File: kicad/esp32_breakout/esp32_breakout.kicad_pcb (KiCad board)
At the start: 2 copper layers, 78 x 39 mm, 30 parts, among them J1 JST PH F, J10 JST PH F, J11 JST PH F, J2 JST PH F, J3 JST PH F, J4 DC-005 5.5x2.1mm, J5 Deans T-Plug M, J6 Header F, J7 Header F, J8 Header F, J9 JST PH F, Q1 BSS123, SW1 SS12D10, U1 ESP32 DEV KIT 30-pin, U2 Mini560-Pro

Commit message: ESP32 breakout v1.0
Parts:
- removed J11: JST PH F, Connector_JST:JST_PH_B6B-PH-K_1x06_P2.00mm_Vertical
- removed the J6 at (123.6, 89.5)
- removed J8: Header F, Connector_PinHeader_2.54mm:PinHeader_1x03_P2.54mm_Vertical
- removed Q1: BSS123, Package_TO_SOT_SMD:SOT-23
- removed R5: 1k, Resistor_SMD:R_0603_1608Metric
- removed R6: 10k, Resistor_SMD:R_0603_1608Metric
- added D2: FS26, Diode_SMD:D_SOD-123F, B.Cu at (188.0, 95.8)
- added F1: FCC20202AATP, Fuse:Fuse_0805_2012Metric, B.Cu at (187.5, 98.0)
- D1: value CGRA4004-G -> FS26; footprint Diode_SMD:D_SMA -> Diode_SMD:D_SOD-123F
- J1, J2: value JST PH F -> JST B5B-PH-K-S
- J10, J9: value JST PH F -> JST B6B-PH-K-S
- J3: value JST PH F -> JST B7B-PH-K-S
- J4: value DC-005 5.5x2.1mm -> J4; footprint Connector_BarrelJack:BarrelJack_GCT_DCJ200-10-A_Horizontal -> Makerspet:AMASS_XT30U-F_1x02_P5.0mm_Vertical
- J5: value Deans T-Plug M -> HDR F 2.54MM VERT; footprint Makerspet:DEANS-T-PLUG -> Connector_PinHeader_2.54mm:PinHeader_1x08_P2.54mm_Vertical; moved to F.Cu
- J6: renamed from J7; value Header F -> HDR F 2.54MM 5-pin VERT
- R10: value 4.7k -> 10k
- R8: moved to F.Cu
- R9: value 100k -> 10k; moved to F.Cu
- U1: value ESP32 DEV KIT 30-pin -> ESP32 DEV KIT Module 30-pin
- U2: value Mini560-Pro -> LM2596 Module; footprint Makerspet:Mini560-Pro -> Makerspet:LM2596 Module
- moved J5 61.8 mm to (127.3, 86.9), turned to 0 degrees
- moved J3 37.9 mm to (174.1, 110.5)
- moved D1 37.0 mm to (134.2, 87.6), turned to -90 degrees
- moved R2 14.8 mm to (171.4, 102.1)
- moved R1 13.3 mm to (171.4, 98.0)
- moved J4 11.6 mm to (192.3, 102.4), turned to 180 degrees
- moved R10 10.4 mm to (171.4, 100.1), turned to 0 degrees
- moved R7 9.97 mm to (161.8, 87.1)
- moved H4 8.92 mm to (128.8, 110.0)
- moved J10 8.35 mm to (180.3, 94.1), turned to -90 degrees
- moved U1 8.30 mm to (151.6, 96.3)
- moved H1 8.00 mm to (128.8, 81.4)
- moved J6 7.24 mm to (134.1, 80.0)
- moved U2 6.52 mm to (150.1, 96.5)
- moved R9 6.32 mm to (166.9, 88.9), turned to 180 degrees
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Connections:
- D1 pad 1: +5V -> Net-(D1-K)
- D1 pad 2: Net-(D1-A) -> +5V
- J3 pad 6: Net-(D1-A) -> unconnected-(J3-Pin_6-Pad6)
- J4 pad 1: +BATT -> GND
- J4 pad 2: GND -> Net-(J4-+)
- J5 pad 1: +BATT -> +5V
- J5 pad 2: GND -> +3V3
- R1 pad 1: /MOT_PWM_LEFT -> +3V3
- R1 pad 2: GND -> /I2C_SCL
- R2 pad 1: /MOT_PWM_RIGHT -> +3V3
- R2 pad 2: GND -> /I2C_INT
- SW1 pad 1: +BATT -> Net-(D2-K)
- U1 pad 30: +5V -> Net-(D1-K)
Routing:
- net +5V: track 129.3 -> 89.3 mm
- net /LDS_MOT_PWM: track 17.2 -> 49.7 mm
- net /LDS_TX: track 5.03 -> 36.4 mm
- net +3V3: track 103.6 -> 75.3 mm
- net /LDS_RX: track 5.22 -> 33.4 mm
- net +BATT: track 21.8 -> 0.00 mm
- net /LDS_MOT_EN: track 12.7 -> 32.9 mm
- net Net-(D1-A): track 13.9 -> 0.00 mm
- net /MOT_CW_RIGHT: track 44.1 -> 33.9 mm
- net /I2C_SDA: track 39.9 -> 30.2 mm
- net /I2C_INT: track 85.9 -> 77.8 mm
- net /GPIO5_BOOT_STRAP: track 26.9 -> 33.8 mm
- net +24V: track 41.3 -> 34.9 mm
- net GND: track 201.9 -> 195.7 mm
- net Net-(J6-Pin_3): track 22.8 -> 28.7 mm
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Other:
- board size 78 x 39 mm -> 70 x 35 mm
- board text added: "BATT"
- board text added: "DIST"
- board text added: "ESP32 Breakout PCB v1.0"
- board text added: "EXT"
- board text added: "LEFT"
- board text added: "LM2596 DC-DC Module"
- board text added: "MOTORS"
- board text added: "OFF"
- board text added: "ON"
- board text added: "RIGHT"
- board text added: "makerspet.com"

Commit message: Socket header
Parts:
- J4: value J4 -> XT30U-M
- J6: footprint Connector_PinHeader_2.54mm:PinHeader_1x05_P2.54mm_Vertical -> Connector_PinSocket_2.54mm:PinSocket_1x05_P2.54mm_Vertical
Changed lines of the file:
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@@
         (effects (font (size 1 1) (thickness 0.15)))
     )
-    (fp_text value "HDR F 2.54MM VERT" (at 2.159 9.652 90) (layer "F.Fab")
+    (fp_text value "HDR F 2.54MM VERT" (at 2.159 9.652 90) (layer "F.Fab") hide
         (effects (font (size 1 1) (thickness 0.15)))
     )
-    (fp_text user "${REFERENCE}" (at 2.54 -1.143) (layer "F.Fab")
+    (fp_text user "${REFERENCE}" (at -0.1016 8.9916) (layer "F.Fab")
         (effects (font (size 1 1) (thickness 0.15)))
     )
@@
         (effects (font (size 1 1) (thickness 0.15)) (justify mirror))
     )
-    (fp_text user "${REFERENCE}" (at -1.35 3.81 -90) (layer "B.Fab")
+    (fp_text user "${REFERENCE}" (at 4.9492 -0.0508 -90) (layer "B.Fab")
         (effects (font (size 1 1) (thickness 0.15)) (justify mirror))
     )
@@
         (effects (font (size 1 1) (thickness 0.15)) (justify mirror))
     )
-    (fp_text user "${REFERENCE}" (at -3.002 -2.794 90) (layer "B.Fab")
+    (fp_text user "${REFERENCE}" (at 3.9576 0 180) (layer "B.Fab")
         (effects (font (size 1 1) (thickness 0.15)) (justify mirror))
     )
@@
         (effects (font (size 1 1) (thickness 0.15)) (justify mirror))
     )
-    (fp_text value "J4" (at -2.032 -3.683) (layer "B.Fab")
+    (fp_text value "XT30U-M" (at 2.6924 -0.1016) (layer "B.Fab") hide
         (effects (font (size 1 1) (thickness 0.15)) (justify mirror))
     )
@@
         (effects (font (size 1.5 1.5) (thickness 0.15)) (justify mirror))
     )
-    (fp_text user "${REFERENCE}" (at -2.032 -3.683) (layer "B.Fab")
+    (fp_text user "${REFERENCE}" (at 2.4384 -0.0508) (layer "B.Fab")
         (effects (font (size 1 1) (thickness 0.15)) (justify mirror))
     )
@@
         (effects (font (size 1 1) (thickness 0.15)) (justify mirror))
     )
-    (fp_text user "${REFERENCE}" (at 15.144 -0.042 90) (layer "B.Fab")
+    (fp_text user "${REFERENCE}" (at 6.1524 0.0088 180) (layer "B.Fab")
         (effects (font (size 1 1) (thickness 0.15)) (justify mirror))
     )
@@
     )
   )
-  (footprint "Connector_PinHeader_2.54mm:PinHeader_1x05_P2.54mm_Vertical" (layer "B.Cu")
+  (footprint "Connector_PinSocket_2.54mm:PinSocket_1x05_P2.54mm_Vertical" (layer "B.Cu")
     (at 134.117 80.01 -90)
-    (descr "Through hole straight pin header, 1x05, 2.54mm pitch, single row")
-    (tags "Through hole pin header THT 1x05 2.54mm single row")
+    (descr "Through hole straight socket strip, 1x05, 2.54mm pitch, single row (from Kicad 4.0.7), script generated")
+    (tags "Through hole socket strip THT 1x05 2.54mm single row")
     (property "Sheetfile" "esp32_breakout.kicad_sch")
     (property "Sheetname" "")
@@
     (property "ki_keywords" "connector")
     (attr through_hole)
-    (fp_text reference "J6" (at 0 -12.949 -180) (layer "B.SilkS")
-        (effects (font (size 1 1) (thickness 0.15)) (justify mirror))
-    )
-    (fp_text value "HDR F 2.54MM 5-pin VERT" (at 0 -12.49 -270) (layer "B.Fab") hide
-        (effects (font (size 1 1) (thickness 0.15)) (justify mirror))
-    )
-    (fp_text user "${REFERENCE}" (at 0 -12.949) (layer "B.Fab")
+    (fp_text reference "J6" (at 0 2.77 90) (layer "B.SilkS")
+        (effects (font (size 1 1) (thickness 0.15)) (justify mirror))
+    )
+    (fp_text value "HDR F 2.54MM 5-pin VERT" (at 0 -12.93 90) (layer "B.Fab") hide
+        (effects (font (size 1 1) (thickness 0.15)) (justify mirror))
+    )
+    (fp_text user "${REFERENCE}" (at 0 -5.08 180) (layer "B.Fab")
         (effects (font (size 1 1) (thickness 0.15)) (justify mirror))
     )
@@
     (fp_line (start -1.33 -1.27) (end 1.33 -1.27)
       (stroke (width 0.12) (type solid)) (layer "B.SilkS"))
-    (fp_line (start -1.33 0) (end -1.33 1.33)
-      (stroke (width 0.12) (type solid)) (layer "B.SilkS"))
-    (fp_line (start -1.33 1.33) (end 0 1.33)
+    (fp_line (start 0 1.33) (end 1.33 1.33)
       (stroke (width 0.12) (type solid)) (layer "B.SilkS"))
     (fp_line (start 1.33 -1.27) (end 1.33 -11.49)
       (stroke (width 0.12) (type solid)) (layer "B.SilkS"))
-    (fp_line (start -1.8 -11.95) (end 1.8 -11.95)
-      (stroke (width 0.05) (type solid)) (layer "B.CrtYd"))
-    (fp_line (start -1.8 1.8) (end -1.8 -11.95)
-      (stroke (width 0.05) (type solid)) (layer "B.CrtYd"))
-    (fp_line (start 1.8 -11.95) (end 1.8 1.8)
-      (stroke (width 0.05) (type solid)) (layer "B.CrtYd"))
-    (fp_line (start 1.8 1.8) (end -1.8 1.8)
-      (stroke (width 0.05) (type solid)) (layer "B.CrtYd"))
-    (fp_line (start -1.27 -11.43) (end -1.27 0.635)
-      (stroke (width 0.1) (type solid)) (layer "B.Fab"))
-    (fp_line (start -1.27 0.635) (end -0.635 1.27)
-      (stroke (width 0.1) (type solid)) (layer "B.Fab"))
-    (fp_line (start -0.635 1.27) (end 1.27 1.27)
+    (fp_line (start 1.33 1.33) (end 1.33 0)
+      (stroke (width 0.12) (type solid)) (layer "B.SilkS"))
+    (fp_line (start -1.8 -11.9) (end -1.8 1.8)
+      (stroke (width 0.05) (type solid)) (layer "B.CrtYd"))
+    (fp_line (start -1.8 1.8) (end 1.75 1.8)
+      (stroke (width 0.05) (type solid)) (layer "B.CrtYd"))
+    (fp_line (start 1.75 -11.9) (end -1.8 -11.9)
+      (stroke (width 0.05) (type solid)) (layer "B.CrtYd"))
+    (fp_line (start 1.75 1.8) (end 1.75 -11.9)
+      (stroke (width 0.05) (type solid)) (layer "B.CrtYd"))
+    (fp_line (start -1.27 -11.43) (end -1.27 1.27)
+      (stroke (width 0.1) (type solid)) (layer "B.Fab"))
+    (fp_line (start -1.27 1.27) (end 0.635 1.27)
+      (stroke (width 0.1) (type solid)) (layer "B.Fab"))
+    (fp_line (start 0.635 1.27) (end 1.27 0.635)
       (stroke (width 0.1) (type solid)) (layer "B.Fab"))
     (fp_line (start 1.27 -11.43) (end -1.27 -11.43)
       (stroke (width 0.1) (type solid)) (layer "B.Fab"))
-    (fp_line (start 1.27 1.27) (end 1.27 -11.43)
+    (fp_line (start 1.27 0.635) (end 1.27 -11.43)
       (stroke (width 0.1) (type solid)) (layer "B.Fab"))
     (pad "1" thru_hole rect (at 0 0 270) (size 1.7 1.7) (drill 1) (layers "*.Cu" "*.Mask")
@@
     (pad "5" thru_hole oval (at 0 -10.16 270) (size 1.7 1.7) (drill 1) (layers "*.Cu" "*.Mask")
       (net 3 "GND") (pinfunction "Pin_5") (pintype "passive"))
-    (model "${KICAD6_3DMODEL_DIR}/Connector_PinHeader_2.54mm.3dshapes/PinHeader_1x05_P2.54mm_Vertical.wrl"
+    (model "${KICAD6_3DMODEL_DIR}/Connector_PinSocket_2.54mm.3dshapes/PinSocket_1x05_P2.54mm_Vertical.wrl"
       (offset (xyz 0 0 0))
       (scale (xyz 1 1 1))
@@
         (effects (font (size 1 1) (thickness 0.15)) (justify mirror))
     )
-    (fp_text user "${REFERENCE}" (at -0.842 -3.81 -90) (layer "B.Fab")
+    (fp_text user "${REFERENCE}" (at 5 0 -90) (layer "B.Fab")
         (effects (font (size 1 1) (thickness 0.15)) (justify mirror))
     )
@@
         (effects (font (size 1 1) (thickness 0.15)) (justify mirror))
     )
-    (fp_text user "${REFERENCE}" (at -3.002 -2.308 90) (layer "B.Fab")
-        (effects (font (size 1 1) (thickness 0.15)) (justify mirror))
-    )
+    (fp_text user "${REFERENCE}" (at 4.0592 0.0288 180) (layer "B.Fab")
+        (effects (font (size 1 1) (thickness 0.15)) (justify mirror))
+    )

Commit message: ESP32 board v1.1
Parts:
- added D3: FS26, Diode_SMD:D_SOD-123F, F.Cu at (178.6, 107.0)
- added Q1: AS2302, Package_TO_SOT_SMD:SOT-23, F.Cu at (184.8, 106.8)
- added R5: 10k, Resistor_SMD:R_0603_1608Metric, F.Cu at (182.1, 107.7)
- added R6: 10k, Resistor_SMD:R_0603_1608Metric, F.Cu at (158.0, 106.7)
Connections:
- J3 pad 2: /LDS_TX -> Net-(J3-Pin_2)
- J3 pad 6: unconnected-(J3-Pin_6-Pad6) -> /LDS_MOT-
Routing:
- net /LDS_TX: track 36.4 -> 12.5 mm
- net Net-(J3-Pin_2): track 0.00 -> 22.0 mm
- net /LDS_MOT-: track 0.00 -> 11.0 mm
- net +5V: track 89.3 -> 95.0 mm
- net /LDS_MOT_PWM: track 49.7 -> 53.9 mm
- net Net-(Q1-G): track 0.00 -> 2.14 mm
- net GND: track 195.7 -> 194.0 mm
- net /GPIO5_BOOT_STRAP: track 33.8 -> 32.4 mm
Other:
- board text added: "ESP32 Breakout PCB v1.1.0"
- board text removed: "ESP32 Breakout PCB v1.0"

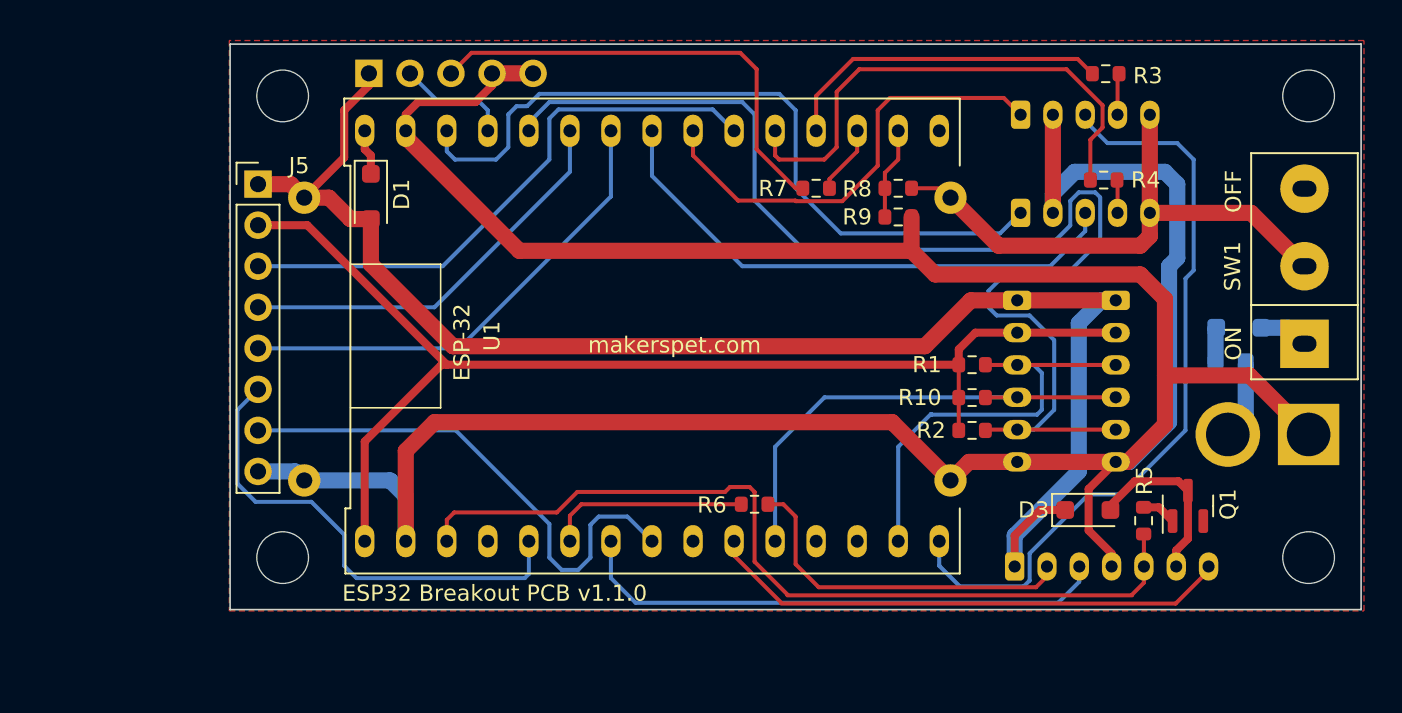
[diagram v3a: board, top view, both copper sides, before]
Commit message: Reverted ESP32 PCB to v1
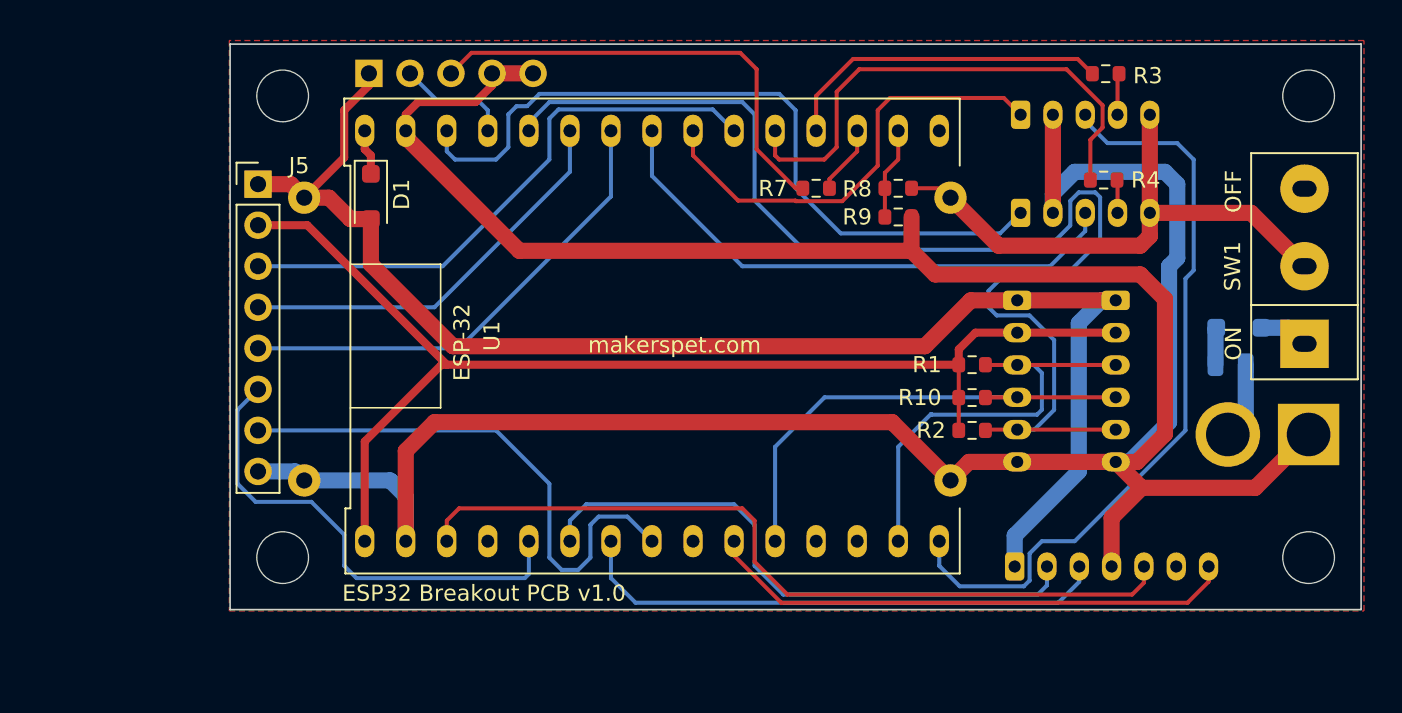
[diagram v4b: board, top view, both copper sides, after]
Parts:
- removed D3: FS26, Diode_SMD:D_SOD-123F
- removed Q1: AS2302, Package_TO_SOT_SMD:SOT-23
- removed R5, R6: 10k, Resistor_SMD:R_0603_1608Metric
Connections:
- J3 pad 2: Net-(J3-Pin_2) -> /LDS_TX
- J3 pad 6: /LDS_MOT- -> unconnected-(J3-Pin_6-Pad6)
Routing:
- net /LDS_TX: track 12.5 -> 36.4 mm
- net Net-(J3-Pin_2): track 22.0 -> 0.00 mm
- net /LDS_MOT-: track 11.0 -> 0.00 mm
- net +5V: track 95.0 -> 89.3 mm
- net /LDS_MOT_PWM: track 53.9 -> 49.7 mm
- net Net-(Q1-G): track 2.14 -> 0.00 mm
- net GND: track 194.0 -> 195.7 mm
- net /GPIO5_BOOT_STRAP: track 32.4 -> 33.8 mm
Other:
- board text added: "ESP32 Breakout PCB v1.0"
- board text removed: "ESP32 Breakout PCB v1.1.0"
